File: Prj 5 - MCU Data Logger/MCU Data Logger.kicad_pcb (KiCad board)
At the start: 2 copper layers, 51.4 x 45.7 mm, 30 parts, among them J1 Conn_01x04_Pin, J2 Conn_01x09_Pin, J3 Conn_01x04_Pin, J4 Conn_02x03_Odd_Even, U1 24LC1025, U2 DS1337S+, U3 24LC1025, U4 ATmega328P, Y1 32.768KHz, Y2 16MHz

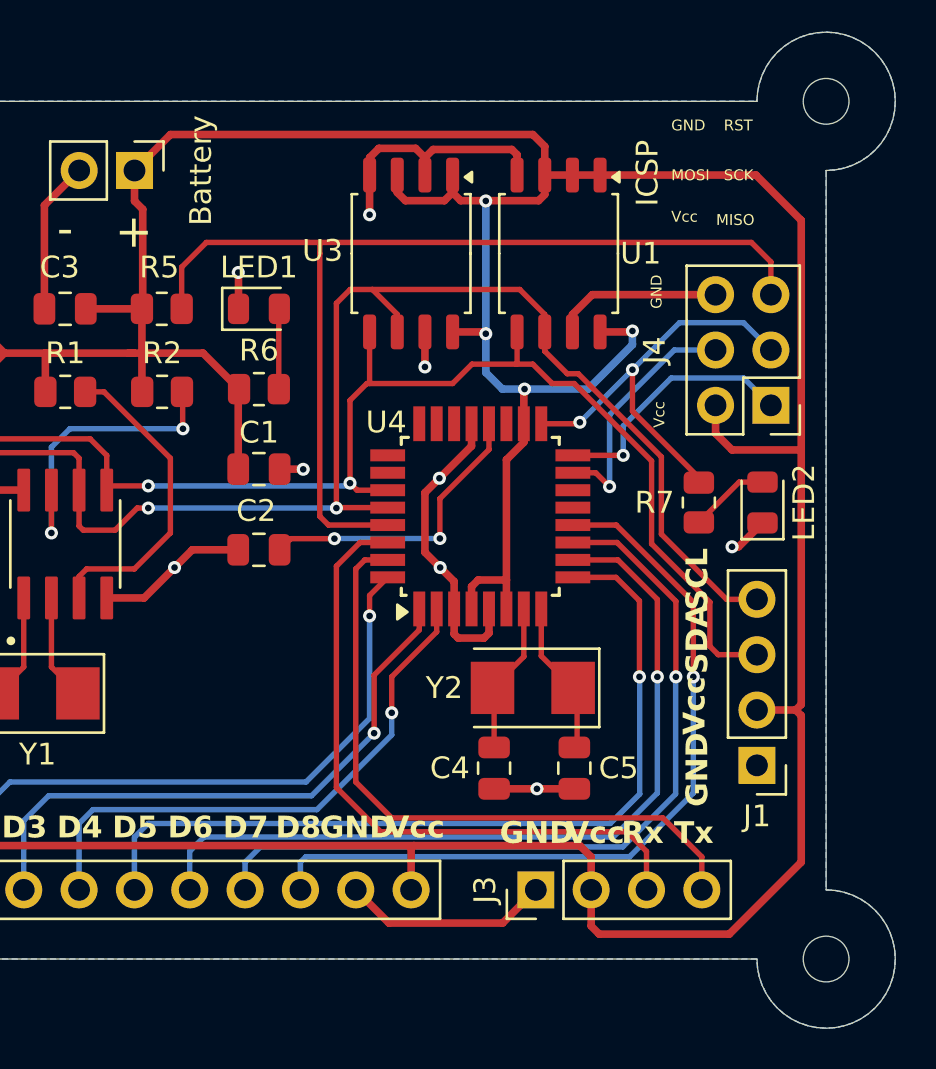
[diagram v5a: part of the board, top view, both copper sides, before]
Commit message: Adjusted Cu2Edge for PCBWay
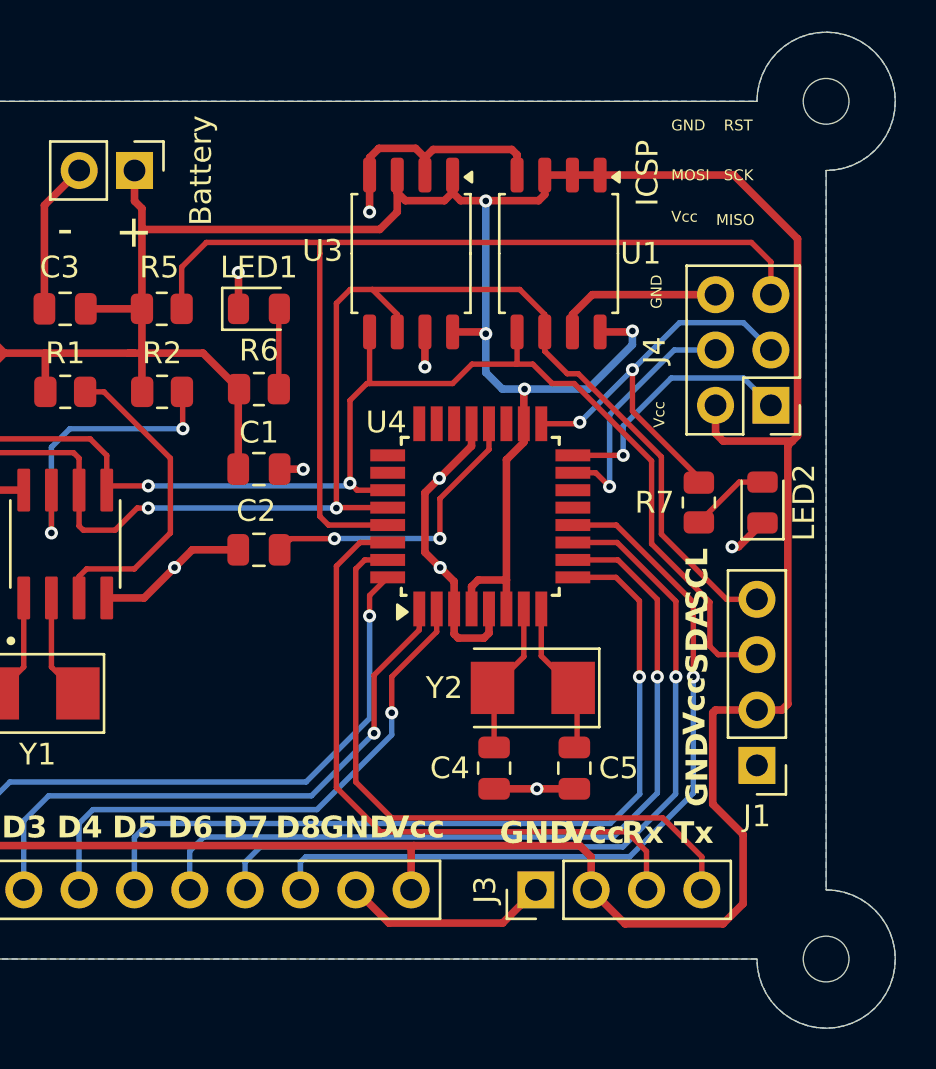
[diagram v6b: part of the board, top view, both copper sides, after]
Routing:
- net /BVcc: track 215.6 -> 206.1 mm
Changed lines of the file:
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@@
 			(outputformat 1)
 			(mirror no)
-			(drillshape 1)
+			(drillshape 0)
 			(scaleselection 1)
-			(outputdirectory "")
+			(outputdirectory "gerber/")
 		)
 	)
@@
 	)
 	(footprint "MountingHole:MountingHole_2.1mm"
-		(locked yes)
 		(layer "F.Cu")
 		(at 175.28 68.395)
@@
 	)
 	(segment
+		(start 155.595 71.78)
+		(end 155.595 73.475)
+		(width 0.35)
+		(layer "F.Cu")
+		(net 1)
+	)
+	(segment
 		(start 159.659 79.063)
 		(end 159.576 78.98)
@@
 	)
 	(segment
+		(start 170.554276 83.989276)
+		(end 173.729276 83.989276)
+		(width 0.35)
+		(layer "F.Cu")
+		(net 1)
+	)
+	(segment
 		(start 143.535 71.57)
 		(end 143.535 72.972)
@@
 	)
 	(segment
-		(start 162.365 71.78)
-		(end 162.365 70.466)
+		(start 173.97 74.705)
+		(end 171.045 71.78)
 		(width 0.35)
 		(layer "F.Cu")
@@
 	)
 	(segment
-		(start 137.561 79.952)
-		(end 136.8225 80.6905)
+		(start 170.075 96.46)
+		(end 170.2 96.335)
 		(width 0.35)
 		(layer "F.Cu")
@@
 	)
 	(segment
-		(start 133.751 87.572)
-		(end 135.083 86.24)
+		(start 173.248 96.335)
+		(end 173.522032 96.060968)
 		(width 0.35)
 		(layer "F.Cu")
@@
 	)
 	(segment
-		(start 164.495 106.251)
-		(end 164.866 106.622)
+		(start 137.561 79.952)
+		(end 136.8225 80.6905)
 		(width 0.35)
 		(layer "F.Cu")
@@
 	)
 	(segment
-		(start 155.970001 72.955)
-		(end 157.759999 72.955)
+		(start 133.751 87.572)
+		(end 135.083 86.24)
 		(width 0.35)
 		(layer "F.Cu")
@@
 	)
 	(segment
-		(start 143.911 73.348)
-		(end 143.911 77.883166)
+		(start 155.970001 72.955)
+		(end 157.759999 72.955)
 		(width 0.35)
 		(layer "F.Cu")
@@
 	)
 	(segment
-		(start 159.659 72.967)
-		(end 159.671 72.955)
+		(start 155.595 73.475)
+		(end 154.793 74.277)
 		(width 0.35)
 		(layer "F.Cu")
@@
 	)
 	(segment
-		(start 163.635 71.78)
-		(end 164.905 71.78)
+		(start 159.659 72.967)
+		(end 159.671 72.955)
 		(width 0.35)
 		(layer "F.Cu")
@@
 	)
 	(segment
-		(start 145.186 69.919)
-		(end 143.535 71.57)
+		(start 163.635 71.78)
+		(end 164.905 71.78)
 		(width 0.35)
 		(layer "F.Cu")
@@
 	)
 	(segment
-		(start 164.495 104.59)
-		(end 164.495 106.231)
-		(width 0.35)
-		(layer "F.Cu")
-		(net 1)
-	)
-	(segment
 		(start 155.595 72.579999)
 		(end 155.970001 72.955)
@@
 	)
 	(segment
-		(start 170.205 83.64)
-		(end 170.962 84.397)
-		(width 0.35)
-		(layer "F.Cu")
-		(net 1)
-	)
-	(segment
 		(start 159.005 90.67)
 		(end 159.309 90.366)
@@
 	)
 	(segment
-		(start 173.883 96.335)
-		(end 174.137 96.081)
-		(width 0.35)
-		(layer "F.Cu")
-		(net 1)
-	)
-	(segment
 		(start 135.083 86.24)
 		(end 138.45 86.24)
@@
 	)
 	(segment
-		(start 172.061 71.78)
-		(end 164.905 71.78)
-		(width 0.35)
-		(layer "F.Cu")
-		(net 1)
-	)
-	(segment
 		(start 139.4425 81.7065)
 		(end 139.4425 81.73)
@@
 	)
 	(segment
-		(start 161.818 69.919)
-		(end 145.186 69.919)
-		(width 0.35)
-		(layer "F.Cu")
-		(net 1)
-	)
-	(segment
 		(start 156.23 102.685)
 		(end 156.357 102.558)
@@
 	)
 	(segment
-		(start 143.535 72.972)
-		(end 143.911 73.348)
-		(width 0.35)
-		(layer "F.Cu")
-		(net 1)
-	)
-	(segment
-		(start 170.835 106.622)
-		(end 174.137 103.32)
+		(start 173.97 83.748552)
+		(end 173.97 74.705)
 		(width 0.35)
 		(layer "F.Cu")
@@
 	)
 	(segment
+		(start 154.793 74.277)
+		(end 143.911 74.277)
+		(width 0.35)
+		(layer "F.Cu")
+		(net 1)
+	)
+	(segment
 		(start 146.6785 79.952)
 		(end 148.3325 81.606)
@@
 	)
 	(segment
-		(start 161.405 81.635)
-		(end 161.437 81.603)
+		(start 171.045 71.78)
+		(end 164.905 71.78)
 		(width 0.35)
 		(layer "F.Cu")
@@
 	)
 	(segment
-		(start 174.137 84.397)
-		(end 174.137 73.856)
+		(start 161.405 81.635)
+		(end 161.437 81.603)
 		(width 0.35)
 		(layer "F.Cu")
@@
 	)
 	(segment
-		(start 162.365 70.466)
-		(end 161.818 69.919)
+		(start 161.437 81.603)
+		(end 161.405 81.571)
 		(width 0.35)
 		(layer "F.Cu")
@@
 	)
 	(segment
-		(start 161.437 81.603)
-		(end 161.405 81.571)
+		(start 161.405 81.571)
+		(end 161.405 81.549325)
 		(width 0.35)
 		(layer "F.Cu")
@@
 	)
 	(segment
-		(start 161.405 81.571)
-		(end 161.405 81.549325)
+		(start 171.47 102.05)
+		(end 170.075 100.655)
 		(width 0.35)
 		(layer "F.Cu")
@@
 	)
 	(segment
-		(start 158.135 72.586)
-		(end 158.504 72.955)
+		(start 173.522032 84.19652)
+		(end 173.729276 83.989276)
 		(width 0.35)
 		(layer "F.Cu")
@@
 	)
 	(segment
-		(start 174.137 73.856)
-		(end 172.061 71.78)
+		(start 173.522032 96.060968)
+		(end 173.522032 84.19652)
+		(width 0.35)
+		(layer "F.Cu")
+		(net 1)
+	)
+	(segment
+		(start 158.135 72.586)
+		(end 158.504 72.955)
 		(width 0.35)
 		(layer "F.Cu")
@@
 	)
 	(segment
-		(start 136.8225 80.6905)
-		(end 136.8225 81.73)
+		(start 170.545014 106.149986)
+		(end 171.47 105.225)
 		(width 0.35)
 		(layer "F.Cu")
@@
 	)
 	(segment
-		(start 139.4425 81.73)
-		(end 139.4425 79.952)
+		(start 136.8225 80.6905)
+		(end 136.8225 81.73)
 		(width 0.35)
 		(layer "F.Cu")
@@
 	)
 	(segment
-		(start 172.105 96.335)
-		(end 173.883 96.335)
+		(start 139.4425 81.73)
+		(end 139.4425 79.952)
 		(width 0.35)
 		(layer "F.Cu")
@@
 	)
 	(segment
-		(start 174.137 96.589)
-		(end 173.883 96.335)
+		(start 170.2 96.335)
+		(end 173.248 96.335)
 		(width 0.35)
 		(layer "F.Cu")
@@
 	)
 	(segment
+		(start 164.495 104.59)
+		(end 166.054986 106.149986)
+		(width 0.35)
+		(layer "F.Cu")
+		(net 1)
+	)
+	(segment
 		(start 166.39 78.936)
 		(end 166.346 78.98)
@@
 	)
 	(segment
-		(start 170.962 84.397)
-		(end 174.137 84.397)
+		(start 170.075 100.655)
+		(end 170.075 96.46)
 		(width 0.35)
 		(layer "F.Cu")
@@
 	)
 	(segment
-		(start 164.866 106.622)
-		(end 170.835 106.622)
+		(start 143.874166 73.311166)
+		(end 143.535 72.972)
+		(width 0.35)
+		(layer "F.Cu")
+		(net 1)
+	)
+	(segment
+		(start 143.874166 77.92)
+		(end 143.874166 73.311166)
 		(width 0.35)
 		(layer "F.Cu")
@@
 	)
 	(segment
+		(start 166.054986 106.149986)
+		(end 170.545014 106.149986)
+		(width 0.35)
+		(layer "F.Cu")
+		(net 1)
+	)
+	(segment
+		(start 173.729276 83.989276)
+		(end 173.97 83.748552)
+		(width 0.35)
+		(layer "F.Cu")
+		(net 1)
+	)
+	(segment
 		(start 164.495 103.076)
 		(end 164.495 104.59)
@@
 	)
 	(segment
-		(start 174.137 103.32)
-		(end 174.137 96.589)
-		(width 0.35)
-		(layer "F.Cu")
-		(net 1)
-	)
-	(segment
 		(start 143.276 79.952)
 		(end 146.6785 79.952)
@@
 	)
 	(segment
-		(start 174.137 96.081)
-		(end 174.137 84.397)
+		(start 166.346 78.98)
+		(end 164.905 78.98)
 		(width 0.35)
 		(layer "F.Cu")
@@
 	)
 	(segment
-		(start 166.346 78.98)
-		(end 164.905 78.98)
+		(start 170.205 83.64)
+		(end 170.554276 83.989276)
 		(width 0.35)
 		(layer "F.Cu")
@@
 	)
 	(segment
+		(start 171.47 105.225)
+		(end 171.47 102.05)
+		(width 0.35)
+		(layer "F.Cu")
+		(net 1)
+	)
+	(segment
 		(start 161.405 84.048)
 		(end 160.605 84.848)
@@
 	)
 	(segment
+		(start 154.325 71.78)
+		(end 154.325 73.475)
+		(width 0.35)
+		(layer "F.Cu")
+		(net 2)
+	)
+	(segment
 		(start 148.3075 76.360955)
 		(end 148.296858 76.350313)
@@
 	)
 	(segment
-		(start 154.325 71.78)
-		(end 154.325 73.602)
-		(width 0.35)
-		(layer "F.Cu")
-		(net 2)
-	)
-	(segment
 		(start 151.286 85.277)
 		(end 151.395 85.277)
@@
 	)
 	(via
-		(at 154.325 73.602)
+		(at 154.325 73.475)
 		(size 0.6)
 		(drill 0.3)
@@
 				(xy 132.17458 70.877315) (xy 132.440064 70.640064) (xy 132.677315 70.37458) (xy 132.883349 70.084202)
 				(xy 133.055576 69.772581) (xy 133.19183 69.443636) (xy 133.290396 69.101504) (xy 133.350036 68.750487)
-				(xy 133.37 68.395)
 			)
 		)

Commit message: Completed 4-layer routing
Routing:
- net /BVcc: track 206.1 -> 9.08 mm, vias 4 -> 0
- net GND: track 67.1 -> 31.2 mm, vias 9 -> 14
- net Net-(U2-SQW/~INT): track 14.0 -> 9.19 mm, vias 2 -> 0
- net /SCL: track 66.2 -> 70.9 mm, vias 2 -> 6
- net Net-(U2-~{INTA}): track 14.6 -> 10.7 mm, vias 0 -> 2
- net /RESET: track 47.2 -> 51.0 mm, vias 0 -> 3
- net /TX: track 30.2 -> 27.0 mm, vias 0 -> 1
- net /SCK: track 19.4 -> 16.4 mm, vias 2 -> 0
- net /SDA: track 63.1 -> 65.7 mm, vias 2 -> 4
- net /D3: track 27.5 -> 29.2 mm, vias 1 -> 2
- net /D4: track 25.7 -> 27.1 mm, vias 1 -> 2
- net /MISO: track 11.9 -> 13.0 mm
- net /RX: track 30.2 -> 31.1 mm, vias 0 -> 1
- net Net-(U4-AREF): track 13.8 -> 14.6 mm, vias 2 -> 0
- net /D2: track 30.3 -> 31.1 mm, vias 1 -> 2
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- added copper zone on F.Cu, net /BVcc
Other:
- copper layers 2 -> 4
- board text added: "MI SO"
- board text added: "MO SI"
- board text removed: "MISO"
- board text removed: "MOSI"
